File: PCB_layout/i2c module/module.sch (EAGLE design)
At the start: 7 parts, among them IC1 ATTINY85-20SU, J1 M20-9980346

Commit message: reorg, i2c dev, lbr updates
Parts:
- removed JP1, JP2, JP3, JP4: (no value), pinhead:PINHD-1X4
- added POWER: (no value), SparkFun-LED:LED3MM
- added R1: 220, SparkFun-Resistors:RESISTORAXIAL-0.3
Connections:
- new net N$11: POWER.A, R1.1
- new net PIN0: IC1.MOSI
- new net PIN1: IC1.MISO
- new net PIN2: IC1.SCK
- net GND: now also R1.2; no longer JP4.1, JP4.2, JP4.3, JP4.4
- net MISO: no longer IC1.MISO
- net PIN3: no longer JP1.1, JP1.2, JP1.3, JP1.4
- net PIN4: no longer JP2.1, JP2.2, JP2.3, JP2.4
- net SCL: no longer IC1.SCK
- net SDA: no longer IC1.MOSI
- net VCC: now also POWER.C; no longer JP3.1, JP3.2, JP3.3, JP3.4
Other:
- moved on the sheet: U$1

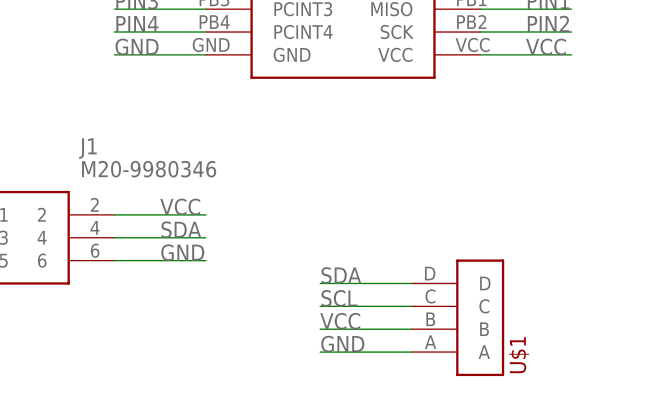
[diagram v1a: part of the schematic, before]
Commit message: made two hema defs
To account for flipping
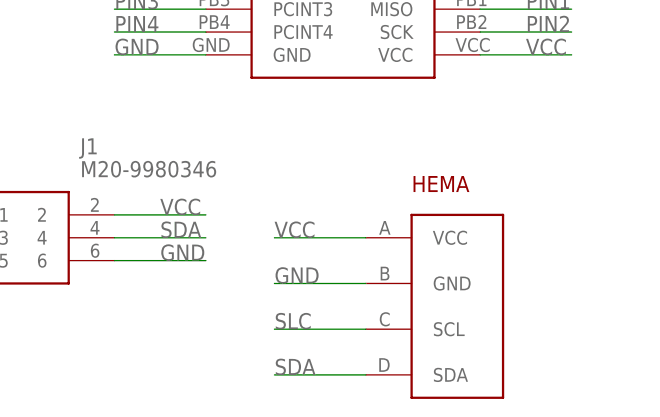
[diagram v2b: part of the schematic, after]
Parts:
- U$1: value 10120045-400LF -> HEMA-I2C; device BadgeParts:10120045-400LF -> BadgeParts:HEMA-I2C
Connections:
- new net SLC: U$1.SCL
- net GND: now also U$1.GND; no longer U$1.A
- net SCL: no longer U$1.C
- net SDA: now also U$1.SDA; no longer U$1.D
- net VCC: now also U$1.VCC; no longer U$1.B
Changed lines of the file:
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@@
 </classes>
 <parts>
-<part name="U$1" library="BadgeParts" deviceset="10120045-400LF" device=""/>
 <part name="IC1" library="BadgeParts" deviceset="ATTINY85-20SU" device=""/>
 <part name="J1" library="BadgeParts" deviceset="M20-9980346" device=""/>
 <part name="R1" library="SparkFun-Resistors" library_urn="urn:adsk.eagle:library:532" deviceset="RESISTOR" device="AXIAL-0.3" package3d_urn="urn:adsk.eagle:package:39658/1" value="220"/>
 <part name="POWER" library="SparkFun-LED" library_urn="urn:adsk.eagle:library:529" deviceset="LED" device="3MM" package3d_urn="urn:adsk.eagle:package:39361/1"/>
+<part name="U$1" library="BadgeParts" deviceset="HEMA-I2C" device=""/>
 </parts>
 <sheets>
@@
 </plain>
 <instances>
-<instance part="U$1" gate="G$1" x="63.5" y="40.64"/>
 <instance part="IC1" gate="G$1" x="35.56" y="83.82"/>
 <instance part="J1" gate="G$1" x="5.08" y="58.42"/>
 <instance part="R1" gate="G$1" x="-5.08" y="96.52"/>
 <instance part="POWER" gate="G$1" x="-12.7" y="96.52" rot="R270"/>
+<instance part="U$1" gate="G$1" x="58.42" y="55.88"/>
 </instances>
 <busses>
@@
 </segment>
 <segment>
-<pinref part="U$1" gate="G$1" pin="D"/>
-<wire x1="58.42" y1="50.8" x2="48.26" y2="50.8" width="0.1524" layer="91"/>
-<label x="48.26" y="50.8" size="1.778" layer="95"/>
+<pinref part="U$1" gate="G$1" pin="SDA"/>
+<wire x1="53.34" y1="40.64" x2="43.18" y2="40.64" width="0.1524" layer="91"/>
+<label x="43.18" y="40.64" size="1.778" layer="95"/>
 </segment>
 </net>
@@
 <label x="-5.08" y="55.88" size="1.778" layer="95"/>
 </segment>
-<segment>
-<pinref part="U$1" gate="G$1" pin="C"/>
-<wire x1="58.42" y1="48.26" x2="48.26" y2="48.26" width="0.1524" layer="91"/>
-<label x="48.26" y="48.26" size="1.778" layer="95"/>
-</segment>
 </net>
 <net name="VCC" class="1">
@@
 <wire x1="25.4" y1="58.42" x2="35.56" y2="58.42" width="0.1524" layer="91"/>
 <label x="30.48" y="58.42" size="1.778" layer="95"/>
-</segment>
-<segment>
-<pinref part="U$1" gate="G$1" pin="B"/>
-<wire x1="58.42" y1="45.72" x2="48.26" y2="45.72" width="0.1524" layer="91"/>
-<label x="48.26" y="45.72" size="1.778" layer="95"/>
 </segment>
 <segment>
@@
 <wire x1="-17.78" y1="96.52" x2="-27.94" y2="96.52" width="0.1524" layer="91"/>
 <label x="-27.94" y="96.52" size="1.778" layer="95"/>
+</segment>
+<segment>
+<pinref part="U$1" gate="G$1" pin="VCC"/>
+<wire x1="53.34" y1="55.88" x2="43.18" y2="55.88" width="0.1524" layer="91"/>
+<label x="43.18" y="55.88" size="1.778" layer="95"/>
 </segment>
 </net>
@@
 </segment>
 <segment>
-<pinref part="U$1" gate="G$1" pin="A"/>
-<wire x1="58.42" y1="43.18" x2="48.26" y2="43.18" width="0.1524" layer="91"/>
-<label x="48.26" y="43.18" size="1.778" layer="95"/>
-</segment>
-<segment>
 <pinref part="J1" gate="G$1" pin="6"/>
 <wire x1="25.4" y1="53.34" x2="35.56" y2="53.34" width="0.1524" layer="91"/>
@@
 <wire x1="0" y1="96.52" x2="12.7" y2="96.52" width="0.1524" layer="91"/>
 <label x="7.62" y="96.52" size="1.778" layer="95"/>
+</segment>
+<segment>
+<pinref part="U$1" gate="G$1" pin="GND"/>
+<wire x1="53.34" y1="50.8" x2="43.18" y2="50.8" width="0.1524" layer="91"/>
+<label x="43.18" y="50.8" size="1.778" layer="95"/>
 </segment>
 </net>
@@
 </segment>
 </net>
+<net name="SLC" class="0">
+<segment>
+<pinref part="U$1" gate="G$1" pin="SCL"/>
+<wire x1="53.34" y1="45.72" x2="43.18" y2="45.72" width="0.1524" layer="91"/>
+<label x="43.18" y="45.72" size="1.778" layer="95"/>
+</segment>
+</net>

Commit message: i2c, lbr updates
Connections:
- removed net MISO: J1.1
- removed net SCL: J1.3
- net PIN1: now also J1.1
- net PIN2: now also J1.3
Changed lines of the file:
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@@
-</segment>
-</net>
-<net name="MISO" class="0">
-<segment>
-<pinref part="J1" gate="G$1" pin="1"/>
-<wire x1="5.08" y1="58.42" x2="-5.08" y2="58.42" width="0.1524" layer="91"/>
-<label x="-5.08" y="58.42" size="1.778" layer="95"/>
-</segment>
-</net>
-<net name="SCL" class="0">
-<segment>
-<pinref part="J1" gate="G$1" pin="3"/>
-<wire x1="5.08" y1="55.88" x2="-5.08" y2="55.88" width="0.1524" layer="91"/>
-<label x="-5.08" y="55.88" size="1.778" layer="95"/>
 </segment>
 </net>
@@
 <label x="71.12" y="81.28" size="1.778" layer="95"/>
 </segment>
+<segment>
+<pinref part="J1" gate="G$1" pin="1"/>
+<wire x1="5.08" y1="58.42" x2="-5.08" y2="58.42" width="0.1524" layer="91"/>
+<label x="-5.08" y="58.42" size="1.778" layer="95"/>
+</segment>
 </net>
 <net name="PIN2" class="0">
@@
 <wire x1="66.04" y1="78.74" x2="76.2" y2="78.74" width="0.1524" layer="91"/>
 <label x="71.12" y="78.74" size="1.778" layer="95"/>
+</segment>
+<segment>
+<pinref part="J1" gate="G$1" pin="3"/>
+<wire x1="5.08" y1="55.88" x2="-5.08" y2="55.88" width="0.1524" layer="91"/>
+<label x="-5.08" y="55.88" size="1.778" layer="95"/>
 </segment>
 </net>
@@
 </drawing>
 <compatibility>
+<note version="6.3" minversion="6.2.2" severity="warning">
+Since Version 6.2.2 text objects can contain more than one line,
+which will not be processed correctly with this version.
+</note>
 <note version="8.2" severity="warning">
 Since Version 8.2, EAGLE supports online libraries. The ids

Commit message: PCB design/lib updates
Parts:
- added 0, 1, 2, 3, 4, 5: 3X-PADS-CONNECTED, BadgeParts:3X-PADS-CONNECTED
- added GND, VCC: 10X-PADS, BadgeParts:10X-PADS
- added P1: PROTO_VIAS_01X01-1.2, dp_devices:PROTO_VIAS_01X01-1.2
- added POWER1: (no value), SparkFun-LED:LED3MM
- added R2: 220, SparkFun-Resistors:RESISTORAXIAL-0.3
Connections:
- removed net PIN0: IC1.MOSI
- removed net PIN1: IC1.MISO, J1.1
- removed net PIN2: IC1.SCK, J1.3
- removed net PIN3: IC1.PCINT3
- removed net PIN4: IC1.PCINT4
- removed net RST: IC1.PCINT5, J1.5
- removed net SDA: J1.4, U$1.SDA
- removed net SLC: U$1.SCL
- new net N$1: POWER1.A, R2.1
- new net N$2: P1.1, R2.2
- new net PB0: 0.P$1, 0.P$2, 0.P$3, IC1.PB0, J1.PB0, U$1.SDA
- new net PB1: IC1.PB1, J1.PB1
- new net PB2: 2.P$1, 2.P$2, 2.P$3, IC1.PB2, J1.PB2, U$1.SCL
- new net PB3: 3.P$1, 3.P$2, 3.P$3, IC1.PB3
- new net PB4: 4.P$1, 4.P$2, 4.P$3, IC1.PB4
- new net PB5: 1.P$1, 1.P$2, 1.P$3, 5.P$1, 5.P$2, 5.P$3, IC1.PB5, J1.PB5
- net GND: now also GND.P$1, GND.P$10, GND.P$2, GND.P$3, GND.P$4, GND.P$5, GND.P$6, GND.P$7, GND.P$8, GND.P$9, J1.GND, POWER.C, POWER1.C; no longer J1.6, R1.2
- net VCC: now also J1.VCC, R1.2, VCC.P$1, VCC.P$10, VCC.P$2, VCC.P$3, VCC.P$4, VCC.P$5, VCC.P$6, VCC.P$7, VCC.P$8, VCC.P$9; no longer J1.2, POWER.C

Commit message: first i2c dongle iteration panelized
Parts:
- added 10, 11, 12, 13, 14, 15, 16, 17, 18, 19, 20, 21, 22, 23, 24, 25, 26, 27, 28, 29, 30, 31, 32, 33, 34, 35, 6, 7, 8, 9: 3X-PADS-CONNECTED, BadgeParts:3X-PADS-CONNECTED
- added GND1, GND2, GND3, GND4, GND5, VCC1, VCC2, VCC3, VCC4, VCC5: 10X-PADS, BadgeParts:10X-PADS
- added IC2, IC3, IC4, IC5, IC6: ATTINY85-20SU, BadgeParts:ATTINY85-20SU
- added J2, J3, J4, J5, J6: M20-9980346, BadgeParts:M20-9980346
- added P2, P3, P4, P5, P6: PROTO_VIAS_01X01-1.2, dp_devices:PROTO_VIAS_01X01-1.2
- added POWER10, POWER11, POWER2, POWER3, POWER4, POWER5, POWER6, POWER7, POWER8, POWER9: (no value), SparkFun-LED:LED3MM
- added R10, R11, R12, R3, R4, R5, R6, R7, R8, R9: 220, SparkFun-Resistors:RESISTORAXIAL-0.3
- added U$2, U$3, U$4, U$5, U$6: HEMA-I2C, BadgeParts:HEMA-I2C
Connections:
- new net N$10: POWER7.A, R8.1
- new net N$12: P4.1, R8.2
- new net N$13: POWER8.A, R9.1
- new net N$14: POWER9.A, R10.1
- new net N$15: P5.1, R10.2
- new net N$16: POWER10.A, R11.1
- new net N$17: POWER11.A, R12.1
- new net N$18: P6.1, R12.2
- new net N$3: POWER2.A, R3.1
- new net N$4: POWER3.A, R4.1
- new net N$5: P2.1, R4.2
- new net N$6: POWER4.A, R5.1
- new net N$7: POWER5.A, R6.1
- new net N$8: P3.1, R6.2
- new net N$9: POWER6.A, R7.1
- net GND: now also GND1.P$1, GND1.P$10, GND1.P$2, GND1.P$3, GND1.P$4, GND1.P$5, GND1.P$6, GND1.P$7, GND1.P$8, GND1.P$9, GND2.P$1, GND2.P$10, GND2.P$2, GND2.P$3, GND2.P$4, GND2.P$5, GND2.P$6, GND2.P$7, GND2.P$8, GND2.P$9, GND3.P$1, GND3.P$10, GND3.P$2, GND3.P$3, GND3.P$4, GND3.P$5, GND3.P$6, GND3.P$7, GND3.P$8, GND3.P$9, GND4.P$1, GND4.P$10, GND4.P$2, GND4.P$3, GND4.P$4, GND4.P$5, GND4.P$6, GND4.P$7, GND4.P$8, GND4.P$9, GND5.P$1, GND5.P$10, GND5.P$2, GND5.P$3, GND5.P$4, GND5.P$5, GND5.P$6, GND5.P$7, GND5.P$8, GND5.P$9, IC2.GND, IC3.GND, IC4.GND, IC5.GND, IC6.GND, J2.GND, J3.GND, J4.GND, J5.GND, J6.GND, POWER10.C, POWER11.C, POWER2.C, POWER3.C, POWER4.C, POWER5.C, POWER6.C, POWER7.C, POWER8.C, POWER9.C, U$2.GND, U$3.GND, U$4.GND, U$5.GND, U$6.GND
- net PB0: now also 10.P$1, 10.P$2, 10.P$3, 16.P$1, 16.P$2, 16.P$3, 22.P$1, 22.P$2, 22.P$3, 28.P$1, 28.P$2, 28.P$3, 34.P$1, 34.P$2, 34.P$3, IC2.PB0, IC3.PB0, IC4.PB0, IC5.PB0, IC6.PB0, J2.PB0, J3.PB0, J4.PB0, J5.PB0, J6.PB0, U$2.SDA, U$3.SDA, U$4.SDA, U$5.SDA, U$6.SDA
- net PB1: now also IC2.PB1, IC3.PB1, IC4.PB1, IC5.PB1, IC6.PB1, J2.PB1, J3.PB1, J4.PB1, J5.PB1, J6.PB1
- net PB2: now also 14.P$1, 14.P$2, 14.P$3, 20.P$1, 20.P$2, 20.P$3, 26.P$1, 26.P$2, 26.P$3, 32.P$1, 32.P$2, 32.P$3, 8.P$1, 8.P$2, 8.P$3, IC2.PB2, IC3.PB2, IC4.PB2, IC5.PB2, IC6.PB2, J2.PB2, J3.PB2, J4.PB2, J5.PB2, J6.PB2, U$2.SCL, U$3.SCL, U$4.SCL, U$5.SCL, U$6.SCL
- net PB3: now also 13.P$1, 13.P$2, 13.P$3, 19.P$1, 19.P$2, 19.P$3, 25.P$1, 25.P$2, 25.P$3, 31.P$1, 31.P$2, 31.P$3, 7.P$1, 7.P$2, 7.P$3, IC2.PB3, IC3.PB3, IC4.PB3, IC5.PB3, IC6.PB3
- net PB4: now also 12.P$1, 12.P$2, 12.P$3, 18.P$1, 18.P$2, 18.P$3, 24.P$1, 24.P$2, 24.P$3, 30.P$1, 30.P$2, 30.P$3, 6.P$1, 6.P$2, 6.P$3, IC2.PB4, IC3.PB4, IC4.PB4, IC5.PB4, IC6.PB4
- net PB5: now also 11.P$1, 11.P$2, 11.P$3, 15.P$1, 15.P$2, 15.P$3, 17.P$1, 17.P$2, 17.P$3, 21.P$1, 21.P$2, 21.P$3, 23.P$1, 23.P$2, 23.P$3, 27.P$1, 27.P$2, 27.P$3, 29.P$1, 29.P$2, 29.P$3, 33.P$1, 33.P$2, 33.P$3, 35.P$1, 35.P$2, 35.P$3, 9.P$1, 9.P$2, 9.P$3, IC2.PB5, IC3.PB5, IC4.PB5, IC5.PB5, IC6.PB5, J2.PB5, J3.PB5, J4.PB5, J5.PB5, J6.PB5
- net VCC: now also IC2.VCC, IC3.VCC, IC4.VCC, IC5.VCC, IC6.VCC, J2.VCC, J3.VCC, J4.VCC, J5.VCC, J6.VCC, R11.2, R3.2, R5.2, R7.2, R9.2, U$2.VCC, U$3.VCC, U$4.VCC, U$5.VCC, U$6.VCC, VCC1.P$1, VCC1.P$10, VCC1.P$2, VCC1.P$3, VCC1.P$4, VCC1.P$5, VCC1.P$6, VCC1.P$7, VCC1.P$8, VCC1.P$9, VCC2.P$1, VCC2.P$10, VCC2.P$2, VCC2.P$3, VCC2.P$4, VCC2.P$5, VCC2.P$6, VCC2.P$7, VCC2.P$8, VCC2.P$9, VCC3.P$1, VCC3.P$10, VCC3.P$2, VCC3.P$3, VCC3.P$4, VCC3.P$5, VCC3.P$6, VCC3.P$7, VCC3.P$8, VCC3.P$9, VCC4.P$1, VCC4.P$10, VCC4.P$2, VCC4.P$3, VCC4.P$4, VCC4.P$5, VCC4.P$6, VCC4.P$7, VCC4.P$8, VCC4.P$9, VCC5.P$1, VCC5.P$10, VCC5.P$2, VCC5.P$3, VCC5.P$4, VCC5.P$5, VCC5.P$6, VCC5.P$7, VCC5.P$8, VCC5.P$9
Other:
- moved on the sheet: POWER, POWER1, R1, R2
